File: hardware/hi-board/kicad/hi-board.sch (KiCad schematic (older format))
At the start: 0 parts

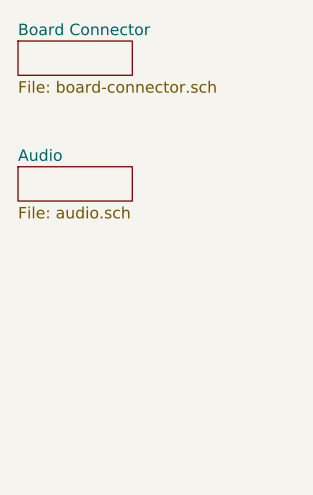
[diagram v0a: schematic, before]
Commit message: Add display and power supply to schematics
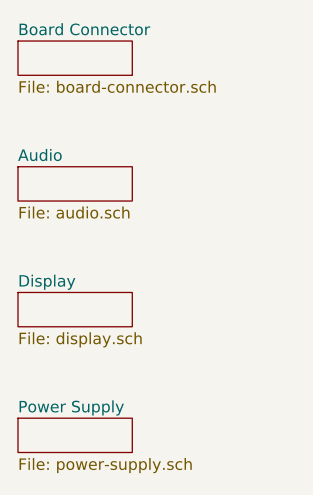
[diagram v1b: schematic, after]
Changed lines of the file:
@@
 $Descr A4 11693 8268
 encoding utf-8
-Sheet 1 3
+Sheet 1 5
 Title "FPGAMB0 (HI Board)"
 Date ""
@@
 F1 "audio.sch" 50
 $EndSheet
+$Sheet
+S 2050 2750 500  150
+U 61420013
+F0 "Display" 50
+F1 "display.sch" 50
+$EndSheet
+$Sheet
+S 2050 3300 500  150
+U 6142C278
+F0 "Power Supply" 50
+F1 "power-supply.sch" 50
+$EndSheet
 $EndSCHEMATC
